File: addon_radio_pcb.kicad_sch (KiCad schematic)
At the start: 4 parts, among them J12 UART Breakout, U10 XBP9B-DMWT-002

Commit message: Add schematic changes from PCB routing/layout
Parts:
- renumbered J12 to J11
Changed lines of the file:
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@@
 		(on_board yes)
 		(dnp no)
-		(property "Reference" "#PWR085"
+		(property "Reference" "#PWR083"
 			(at 127 36.83 0)
 			(effects
@@
 			(project "nerve_pcb"
 				(path "/c0277862-b3f2-4e0e-986f-34702f0543f0/c74e3869-b9cc-416c-ac24-f158c9a16ca3"
-					(reference "#PWR085")
+					(reference "#PWR083")
 					(unit 1)
 				)
@@
 		(dnp no)
 		(fields_autoplaced yes)
-		(property "Reference" "#PWR084"
+		(property "Reference" "#PWR082"
 			(at 78.74 36.83 0)
 			(effects
@@
 			(project "nerve_pcb"
 				(path "/c0277862-b3f2-4e0e-986f-34702f0543f0/c74e3869-b9cc-416c-ac24-f158c9a16ca3"
-					(reference "#PWR084")
+					(reference "#PWR082")
 					(unit 1)
 				)
@@
 		(dnp no)
 		(fields_autoplaced yes)
-		(property "Reference" "#PWR086"
+		(property "Reference" "#PWR084"
 			(at 127 49.53 0)
 			(effects
@@
 			(project "nerve_pcb"
 				(path "/c0277862-b3f2-4e0e-986f-34702f0543f0/c74e3869-b9cc-416c-ac24-f158c9a16ca3"
-					(reference "#PWR086")
+					(reference "#PWR084")
 					(unit 1)
 				)
@@
 		(dnp no)
 		(fields_autoplaced yes)
-		(property "Reference" "#PWR087"
+		(property "Reference" "#PWR085"
 			(at 59.69 88.9 0)
 			(effects
@@
 			(project "nerve_pcb"
 				(path "/c0277862-b3f2-4e0e-986f-34702f0543f0/c74e3869-b9cc-416c-ac24-f158c9a16ca3"
-					(reference "#PWR087")
+					(reference "#PWR085")
 					(unit 1)
 				)
@@
 		(on_board yes)
 		(dnp no)
-		(property "Reference" "J12"
+		(property "Reference" "J11"
 			(at 134.366 36.576 0)
 			(effects
@@
 			(project "nerve_pcb"
 				(path "/c0277862-b3f2-4e0e-986f-34702f0543f0/c74e3869-b9cc-416c-ac24-f158c9a16ca3"
-					(reference "J12")
+					(reference "J11")
 					(unit 1)
 				)
@@
 		(on_board yes)
 		(dnp no)
-		(property "Reference" "#PWR083"
+		(property "Reference" "#PWR081"
 			(at 78.74 21.59 0)
 			(effects
@@
 			(project "nerve_pcb"
 				(path "/c0277862-b3f2-4e0e-986f-34702f0543f0/c74e3869-b9cc-416c-ac24-f158c9a16ca3"
-					(reference "#PWR083")
-					(unit 1)
-				)
+					(reference "#PWR081")
+					(unit 1)
+				)

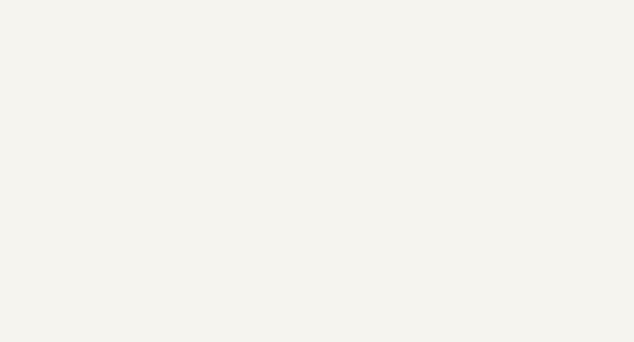
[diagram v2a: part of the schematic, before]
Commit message: Add mounting holes to secondary schematics
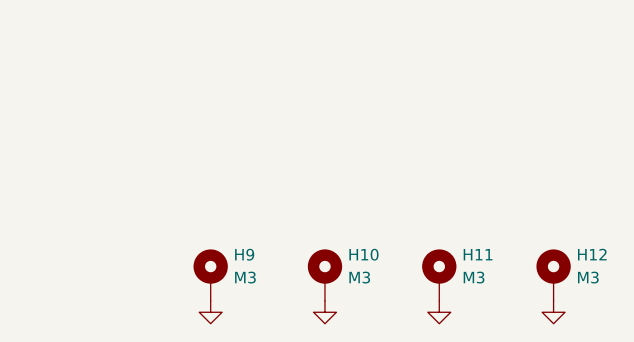
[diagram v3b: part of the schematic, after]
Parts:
- added H10, H11, H12, H9: M3, MountingHole:MountingHole_3.2mm_M3_Pad_Via, symbol Mechanical:MountingHole_Pad
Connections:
- net GND: now also H10.1, H11.1, H12.1, H9.1

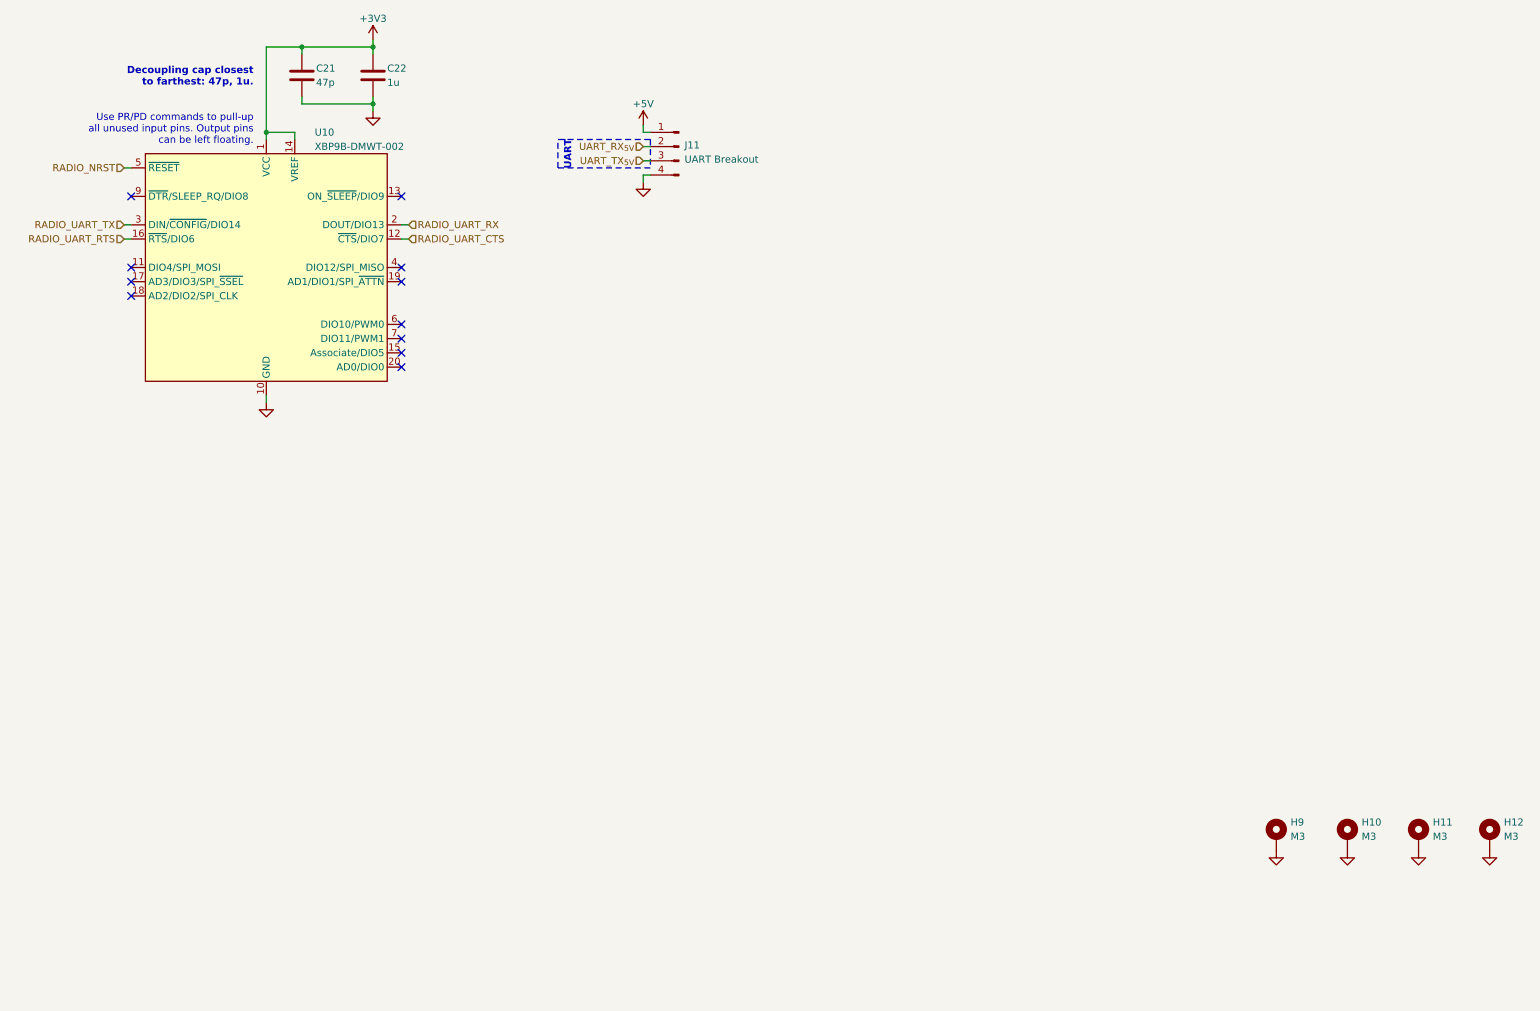
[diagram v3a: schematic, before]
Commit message: Update schematics for add-on PCB separation
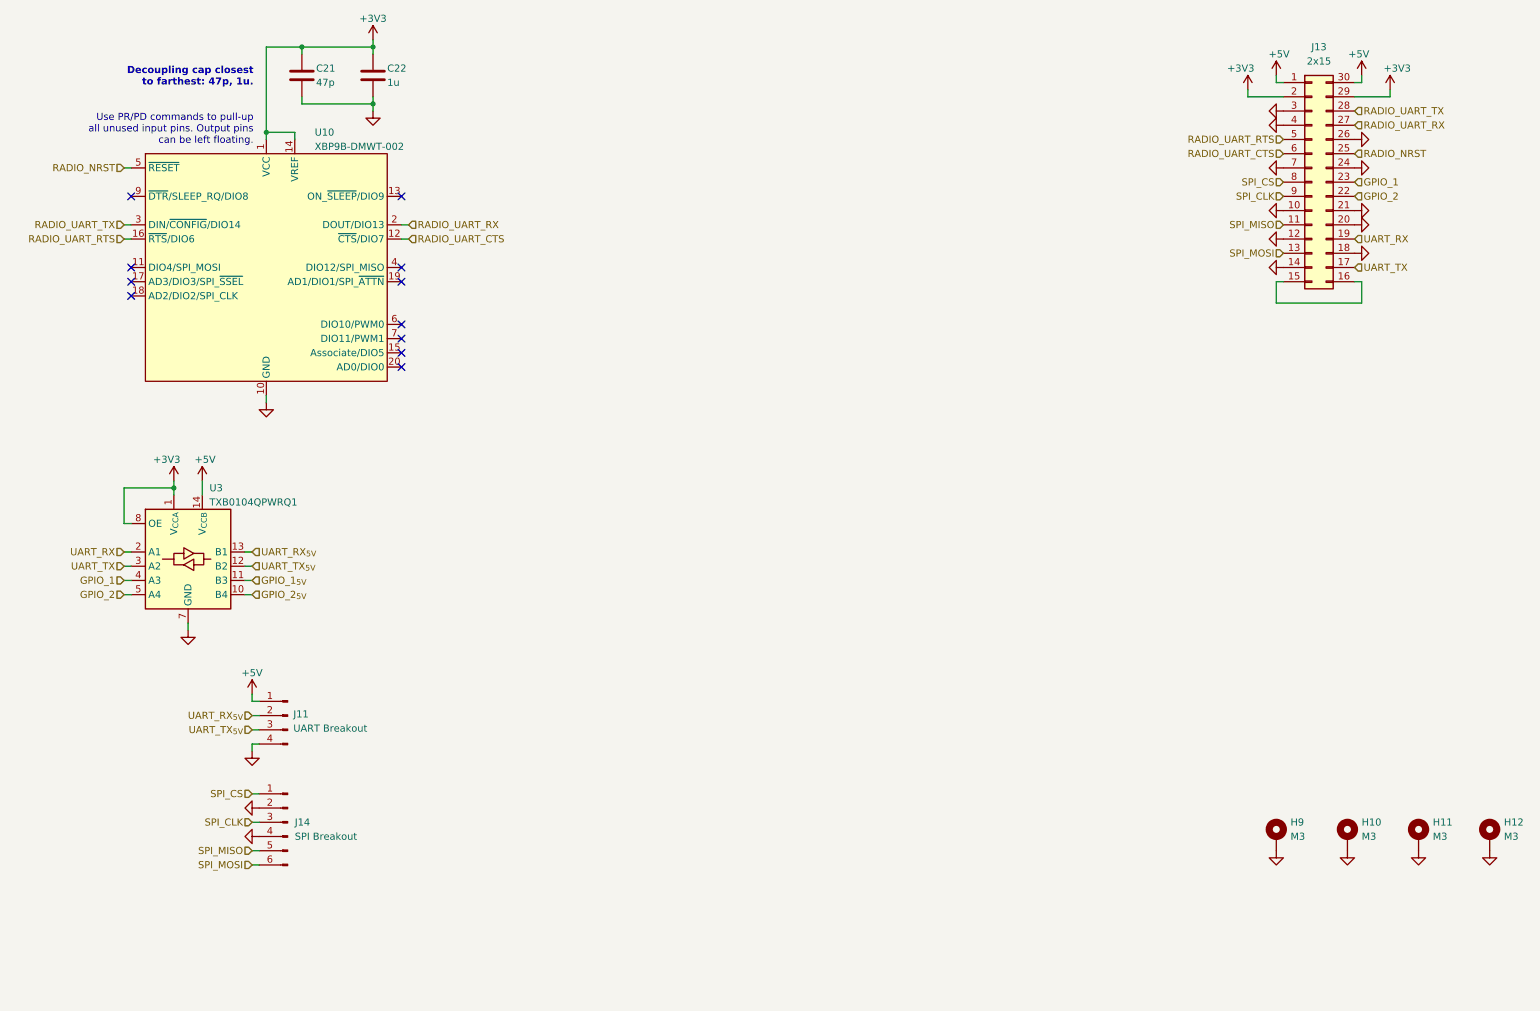
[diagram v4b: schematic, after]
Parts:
- added J13: 2x15, symbol Connector_Generic:Conn_02x15_Counter_Clockwise
- added J14: SPI Breakout, symbol Connector:Conn_01x06_Pin
- added U3: TXB0104QPWRQ1, common:txb0104qpwrq1, symbol common:txb0104qpwrq1
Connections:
- net +3V3: now also J13.2 (Pin_2), J13.29 (Pin_29), U3.1 (V_{CCA}), U3.8 (OE)
- net +5V: now also J13.1 (Pin_1), J13.30 (Pin_30), U3.14 (V_{CCB})
- net GND: now also J13.10 (Pin_10), J13.12 (Pin_12), J13.14 (Pin_14), J13.18 (Pin_18), J13.20 (Pin_20), J13.21 (Pin_21), J13.24 (Pin_24), J13.26 (Pin_26), J13.3 (Pin_3), J13.4 (Pin_4), J13.7 (Pin_7), J14.2 (Pin_2), J14.4 (Pin_4), U3.7 (GND)
- net RADIO_NRST: now also J13.25 (Pin_25)
- net RADIO_UART_CTS: now also J13.6 (Pin_6)
- net RADIO_UART_RTS: now also J13.5 (Pin_5)
- net RADIO_UART_RX: now also J13.27 (Pin_27)
- net RADIO_UART_TX: now also J13.28 (Pin_28)
- net UART_RX_{5V}: now also U3.13 (B1)
- net UART_TX_{5V}: now also U3.12 (B2)
- new net: J13.15 (Pin_15), J13.16 (Pin_16)
- new net GPIO_1: J13.23 (Pin_23), U3.4 (A3)
- new net GPIO_1_{5V}: U3.11 (B3)
- new net GPIO_2: J13.22 (Pin_22), U3.5 (A4)
- new net GPIO_2_{5V}: U3.10 (B4)
- new net SPI_CLK: J13.9 (Pin_9), J14.3 (Pin_3)
- new net SPI_CS: J13.8 (Pin_8), J14.1 (Pin_1)
- new net SPI_MISO: J13.11 (Pin_11), J14.5 (Pin_5)
- new net SPI_MOSI: J13.13 (Pin_13), J14.6 (Pin_6)
- new net UART_RX: J13.19 (Pin_19), U3.2 (A1)
- new net UART_TX: J13.17 (Pin_17), U3.3 (A2)
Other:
- moved on the sheet: J11

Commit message: Update refs on schematics
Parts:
- renumbered J13 to J11, J11 to J12, J14 to J13, U3 to U10, U10 to U9

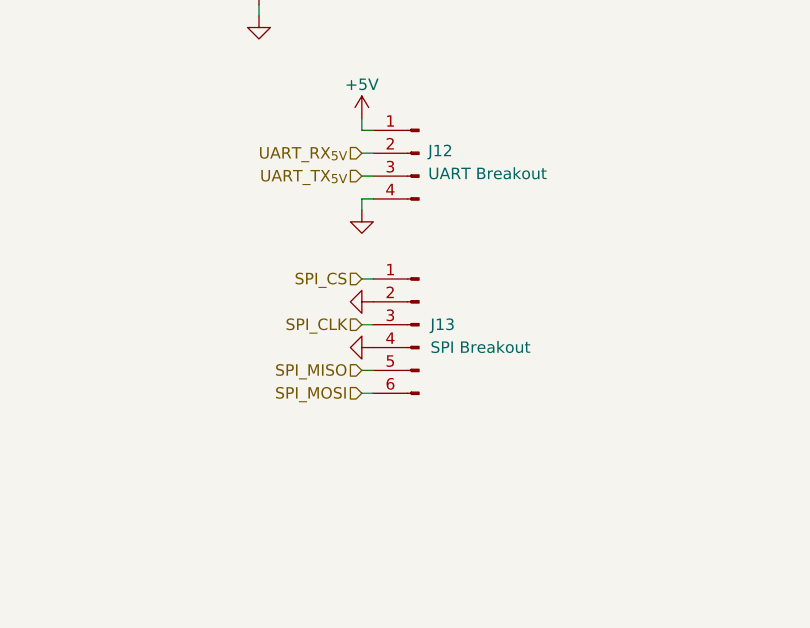
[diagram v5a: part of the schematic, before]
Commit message: Add breakout connectors to add-on PCBs
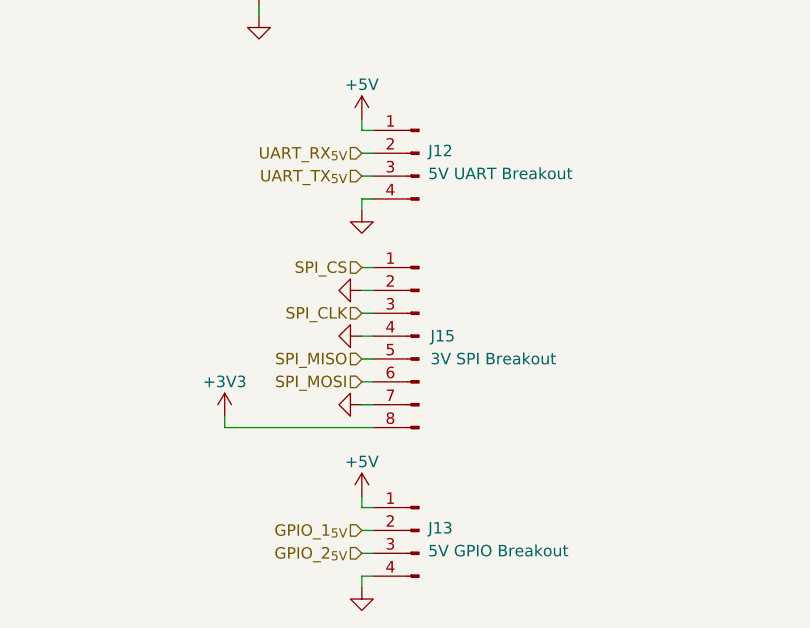
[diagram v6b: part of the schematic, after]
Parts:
- removed J13: SPI Breakout, symbol Connector:Conn_01x06_Pin
- added J13: 5V GPIO Breakout, Connector_PinHeader_2.54mm:PinHeader_1x04_P2.54mm_Vertical, symbol Connector:Conn_01x04_Pin
- added J15: 3V SPI Breakout, symbol Connector:Conn_01x08_Pin
- J12: value UART Breakout -> 5V UART Breakout
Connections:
- net +3V3: now also J15.8 (Pin_8)
- net +5V: now also J13.1 (Pin_1)
- net GND: now also J13.4 (Pin_4), J15.2 (Pin_2), J15.4 (Pin_4), J15.7 (Pin_7)
- net GPIO_1_{5V}: now also J13.2 (Pin_2)
- net GPIO_2_{5V}: now also J13.3 (Pin_3)
- net SPI_CLK: now also J15.3 (Pin_3)
- net SPI_CS: now also J15.1 (Pin_1)
- net SPI_MISO: now also J15.5 (Pin_5)
- net SPI_MOSI: now also J15.6 (Pin_6)

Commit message: Clean up schematics and add footprints
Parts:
- J12: renamed from J11; footprint (none) -> Connector_PinHeader_2.54mm:PinHeader_2x15_P2.54mm_Vertical
- J14: renamed from J15; footprint (none) -> Connector_PinHeader_2.54mm:PinHeader_1x08_P2.54mm_Vertical
- renumbered J12 to J13, J13 to J15

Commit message: Swap to 1.27mm board-to-board and WIP PCB
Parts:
- J12: footprint Connector_PinHeader_2.54mm:PinHeader_2x15_P2.54mm_Vertical -> Connector_PinHeader_1.27mm:PinHeader_2x15_P1.27mm_Vertical_SMD
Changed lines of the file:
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@@
 			)
 		)
-		(property "Footprint" "Connector_PinHeader_2.54mm:PinHeader_2x15_P2.54mm_Vertical"
+		(property "Footprint" "Connector_PinHeader_1.27mm:PinHeader_2x15_P1.27mm_Vertical_SMD"
 			(at 246.38 43.18 0)
 			(effects
